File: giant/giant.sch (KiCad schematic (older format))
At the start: 55 parts, among them IC1 MC7805BDTRKG, J1 Conn_01x02, J2 Conn_01x01, J3 Conn_01x06

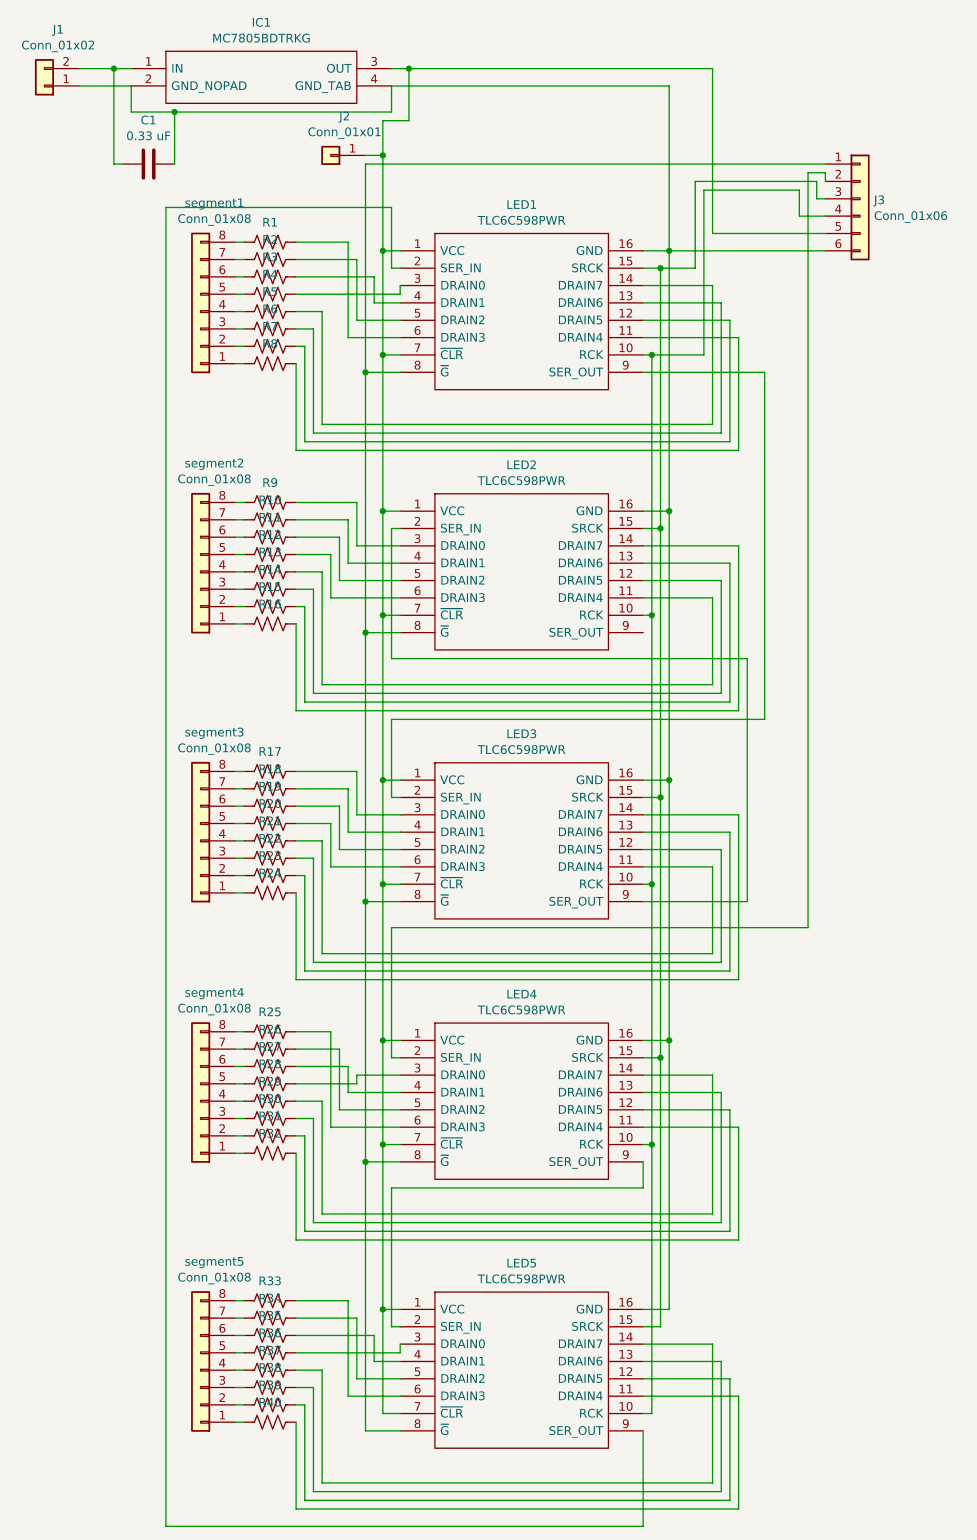
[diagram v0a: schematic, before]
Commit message: Improved schematic layout for both cleanliness and programming ease
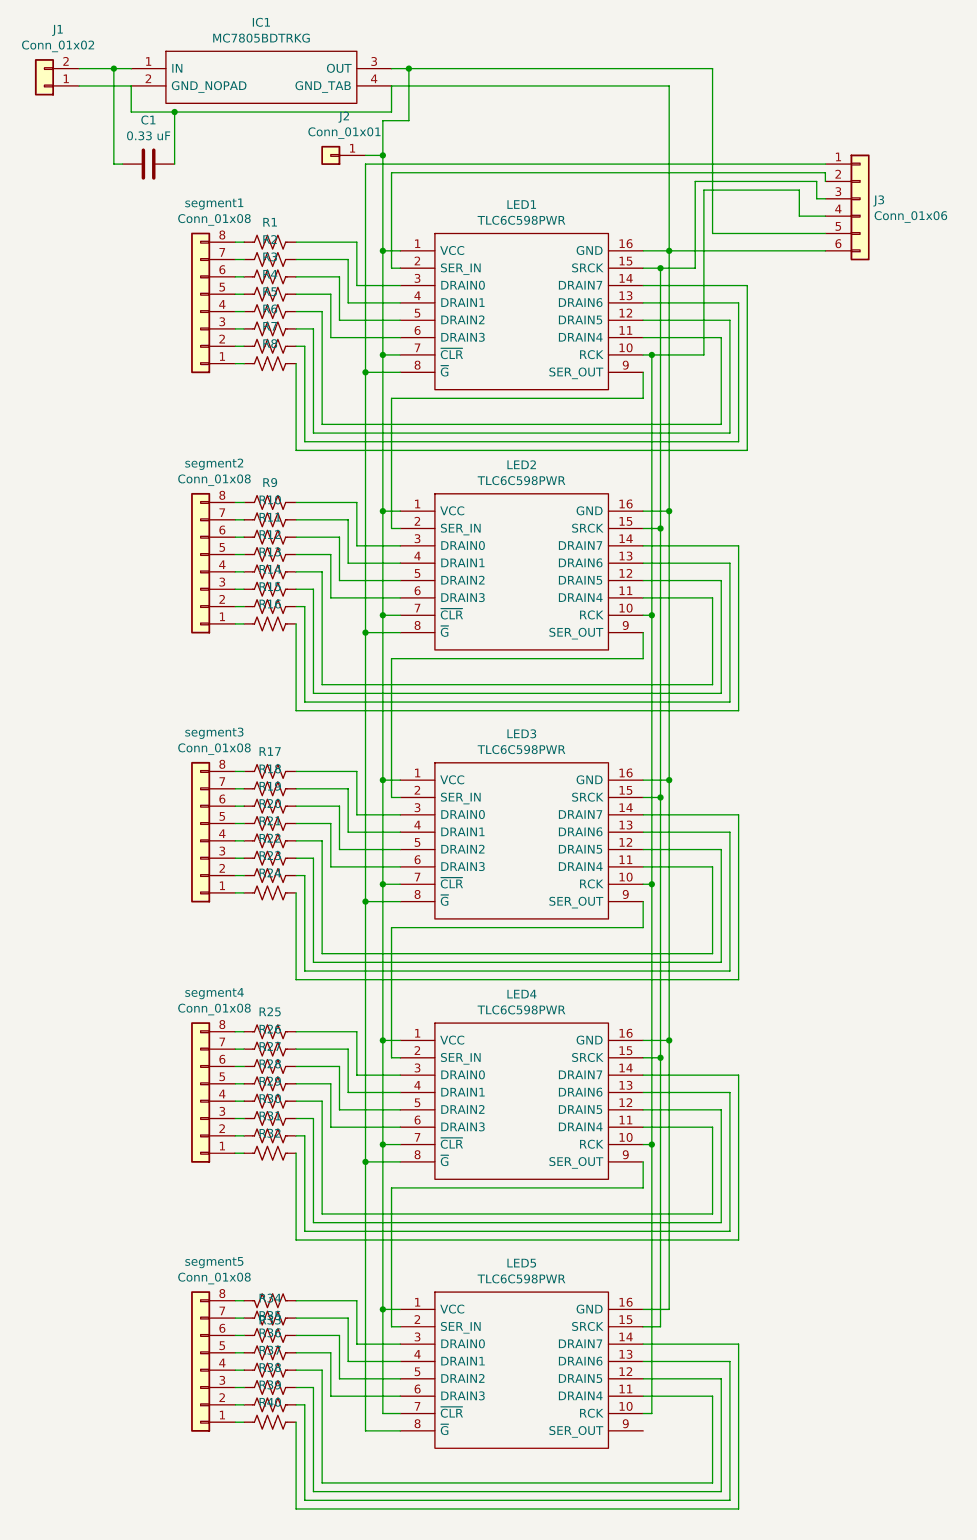
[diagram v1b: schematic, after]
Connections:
- net at LED5.11 (DRAIN4): now also R37.2; no longer R40.2
- net at LED5.12 (DRAIN5): now also R38.2; no longer R39.2
- net at LED5.13 (DRAIN6): now also R39.2; no longer R38.2
- net at LED5.14 (DRAIN7): now also R40.2; no longer R37.2
- net at LED5.3 (DRAIN0): now also R33.2; no longer R36.2
- net at LED5.4 (DRAIN1): now also R34.2; no longer R35.2
- net at LED5.5 (DRAIN2): now also R35.2; no longer R34.2
- net at LED5.6 (DRAIN3): now also R36.2; no longer R33.2
- net at LED5.9 (SER_OUT): no longer LED1.2 (SER_IN)
- net at LED4.11 (DRAIN4): now also R29.2; no longer R32.2
- net at LED4.12 (DRAIN5): now also R30.2; no longer R31.2
- net at LED4.13 (DRAIN6): now also R31.2; no longer R30.2
- net at LED4.14 (DRAIN7): now also R32.2; no longer R29.2
- net at LED4.2 (SER_IN): now also LED3.9 (SER_OUT); no longer J3.2 (Pin_2)
- net at LED4.3 (DRAIN0): now also R25.2; no longer R28.2
- net at LED4.4 (DRAIN1): now also R26.2; no longer R27.2
- net at LED4.5 (DRAIN2): now also R27.2; no longer R26.2
- net at LED4.6 (DRAIN3): now also R28.2; no longer R25.2
- net at LED3.2 (SER_IN): now also LED2.9 (SER_OUT); no longer LED1.9 (SER_OUT)
- net at LED2.2 (SER_IN): now also LED1.9 (SER_OUT); no longer LED3.9 (SER_OUT)
- net at LED1.11 (DRAIN4): now also R5.2; no longer R8.2
- net at LED1.12 (DRAIN5): now also R6.2; no longer R7.2
- net at LED1.13 (DRAIN6): now also R7.2; no longer R6.2
- net at LED1.14 (DRAIN7): now also R8.2; no longer R5.2
- net at LED1.3 (DRAIN0): now also R1.2; no longer R4.2
- net at LED1.4 (DRAIN1): now also R2.2; no longer R3.2
- net at LED1.5 (DRAIN2): now also R3.2; no longer R2.2
- net at LED1.6 (DRAIN3): now also R4.2; no longer R1.2
- new net: J3.2 (Pin_2), LED1.2 (SER_IN)
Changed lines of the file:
@@
 EESchema Schematic File Version 4
+LIBS:giant-cache
 EELAYER 26 0
 EELAYER END
@@
 Wire Wire Line
 	4100 8700 4100 8100
-$Comp
-L TLC6C598PWR:TLC6C598PWR LED4
-U 1 1 5C3858CA
-P 4200 6550
-F 0 "LED4" H 4900 6815 50  0000 C CNN
-F 1 "TLC6C598PWR" H 4900 6724 50  0000 C CNN
-F 2 "SOP65P640X120-16N" H 5450 6650 50  0001 L CNN
-F 3 "http://www.ti.com/lit/gpn/tlc6c598" H 5450 6550 50  0001 L CNN
-F 4 "TLC6C598 8-Bit Shift-Register LED Driver " H 5450 6450 50  0001 L CNN "Description"
-F 5 "1.2" H 5450 6350 50  0001 L CNN "Height"
-F 6 "Texas Instruments" H 5450 6250 50  0001 L CNN "Manufacturer_Name"
-F 7 "TLC6C598PWR" H 5450 6150 50  0001 L CNN "Manufacturer_Part_Number"
-F 8 "595-TLC6C598PWR" H 5450 5850 50  0001 L CNN "Mouser Part Number"
-F 9 "https://www.mouser.com/Search/Refine.aspx?Keyword=595-TLC6C598PWR" H 5450 5750 50  0001 L CNN "Mouser Price/Stock"
-	1    4200 6550
-	1    0    0    -1
-$EndComp
 Wire Wire Line
 	4200 6550 4100 6550
@@
 Connection ~ 4000 7250
 Wire Wire Line
-	4200 8200 4150 8200
-Wire Wire Line
-	4150 8200 4150 7400
-Wire Wire Line
-	4150 7400 5600 7400
-Wire Wire Line
-	5600 7400 5600 7250
-Wire Wire Line
-	4200 6650 4150 6650
-Wire Wire Line
-	4150 6650 4150 5900
-Wire Wire Line
 	4200 5150 4150 5150
-Wire Wire Line
-	4150 5150 4150 4700
 Wire Wire Line
 	5600 2600 5650 2600
@@
 	3300 1950 3250 1950
 Wire Wire Line
-	6000 3000 3750 3000
-Wire Wire Line
 	3750 3000 3750 2350
 Wire Wire Line
 	3750 2350 3600 2350
 Wire Wire Line
-	6050 3050 3700 3050
-Wire Wire Line
 	3700 3050 3700 2450
 Wire Wire Line
@@
 Wire Wire Line
 	3650 2550 3600 2550
-Wire Wire Line
-	3650 3100 6100 3100
 Connection ~ 4100 3500
 Connection ~ 4100 2600
@@
 Wire Wire Line
 	4000 1500 4000 2700
-Wire Wire Line
-	6150 3150 3600 3150
 Wire Wire Line
 	3600 3150 3600 2650
@@
 	3300 6500 3250 6500
 Wire Wire Line
-	3950 6750 4200 6750
-Wire Wire Line
-	4200 6850 3900 6850
-Wire Wire Line
-	3850 6950 4200 6950
-Wire Wire Line
-	4200 7050 3800 7050
-Wire Wire Line
 	3750 7550 3750 6900
 Wire Wire Line
@@
 F 4 "ESR10EZPJ201" H 3450 8050 50  0001 C CNN "PartNumber"
 	1    3450 8050
-	0    -1   -1   0
+	0    -1   1    0
 $EndComp
 $Comp
@@
 	4000 1500 6650 1500
 Wire Wire Line
-	6650 1550 6650 1600
-Wire Wire Line
 	6600 1600 6600 1700
 Wire Wire Line
@@
 	4100 1450 4100 2000
 Wire Wire Line
-	3800 6500 3600 6500
-Wire Wire Line
-	3800 6500 3800 7050
-Wire Wire Line
-	3850 6950 3850 6600
-Wire Wire Line
-	3850 6600 3600 6600
-Wire Wire Line
-	3900 6850 3900 6700
-Wire Wire Line
-	3900 6700 3600 6700
-Wire Wire Line
-	3950 6750 3950 6800
-Wire Wire Line
-	3950 6800 3600 6800
-Wire Wire Line
-	6000 6750 5600 6750
-Wire Wire Line
-	6000 6750 6000 7550
-Wire Wire Line
-	6050 7600 6050 6850
-Wire Wire Line
-	6050 6850 5600 6850
-Wire Wire Line
-	6100 7650 6100 6950
-Wire Wire Line
-	6100 6950 5600 6950
-Wire Wire Line
-	6150 7700 6150 7050
-Wire Wire Line
-	6150 7050 5600 7050
-Wire Wire Line
-	6000 9100 6000 8300
-Wire Wire Line
-	6000 8300 5600 8300
-Wire Wire Line
-	6050 9150 6050 8400
-Wire Wire Line
-	6050 8400 5600 8400
-Wire Wire Line
-	6100 9200 6100 8500
-Wire Wire Line
-	6100 8500 5600 8500
-Wire Wire Line
-	6150 9250 6150 8600
-Wire Wire Line
-	6150 8600 5600 8600
-Wire Wire Line
-	4200 8300 4200 8350
-Wire Wire Line
-	4200 8350 3600 8350
-Wire Wire Line
-	4200 8400 4050 8400
-Wire Wire Line
-	4050 8400 4050 8250
-Wire Wire Line
-	4050 8250 3600 8250
-Wire Wire Line
-	4200 8500 3950 8500
-Wire Wire Line
-	3950 8500 3950 8150
-Wire Wire Line
-	3950 8150 3600 8150
-Wire Wire Line
-	4200 8600 3900 8600
-Wire Wire Line
-	3900 8600 3900 8050
-Wire Wire Line
-	3900 8050 3600 8050
-Wire Wire Line
 	4200 5250 3950 5250
 Wire Wire Line
@@
 Wire Wire Line
 	3800 3750 3600 3750
-Wire Wire Line
-	4200 2200 4200 2250
-Wire Wire Line
-	4050 2300 4050 2150
-Wire Wire Line
-	4200 2300 4050 2300
-Wire Wire Line
-	4200 2500 3900 2500
-Wire Wire Line
-	4200 2400 3950 2400
-Wire Wire Line
-	3900 1950 3600 1950
-Wire Wire Line
-	3900 2500 3900 1950
-Wire Wire Line
-	3950 2050 3600 2050
-Wire Wire Line
-	3950 2400 3950 2050
-Wire Wire Line
-	4050 2150 3600 2150
-Wire Wire Line
-	4200 2250 3600 2250
-Wire Wire Line
-	6000 2200 5600 2200
-Wire Wire Line
-	6000 3000 6000 2200
-Wire Wire Line
-	6050 2300 5600 2300
-Wire Wire Line
-	6050 3050 6050 2300
-Wire Wire Line
-	6100 2400 5600 2400
-Wire Wire Line
-	6100 3100 6100 2400
-Wire Wire Line
-	6150 2500 6150 3150
-Wire Wire Line
-	5600 2500 6150 2500
-Wire Wire Line
-	5600 8800 5600 9350
-Wire Wire Line
-	5600 9350 2850 9350
-Wire Wire Line
-	2850 1750 2850 9350
-Wire Wire Line
-	4150 1750 4150 2100
-Wire Wire Line
-	4150 2100 4200 2100
-Wire Wire Line
-	2850 1750 4150 1750
 $Comp
 L TLC6C598PWR:TLC6C598PWR LED1
@@
 $EndComp
 Wire Wire Line
-	5600 2700 6300 2700
-Wire Wire Line
-	6300 2700 6300 4700
-Wire Wire Line
-	6300 4700 4150 4700
-Wire Wire Line
-	5600 5750 6200 5750
-Wire Wire Line
-	6200 5750 6200 4350
-Wire Wire Line
-	6200 4350 4150 4350
-Wire Wire Line
-	4150 4350 4150 3600
-Wire Wire Line
-	4150 3600 4200 3600
-Wire Wire Line
-	6550 5900 6550 1550
-Wire Wire Line
-	6550 1550 6650 1550
-Wire Wire Line
-	4150 5900 6550 5900
-Wire Wire Line
 	5750 1050 5750 2000
 Wire Wire Line
@@
 Wire Wire Line
 	5750 2000 6650 2000
+Wire Wire Line
+	3750 3000 6050 3000
+Wire Wire Line
+	5600 2500 6050 2500
+Wire Wire Line
+	6050 2500 6050 3000
+Wire Wire Line
+	6100 3050 6100 2400
+Wire Wire Line
+	6100 2400 5600 2400
+Wire Wire Line
+	3700 3050 6100 3050
+Wire Wire Line
+	5600 2300 6150 2300
+Wire Wire Line
+	6150 2300 6150 3100
+Wire Wire Line
+	3650 3100 6150 3100
+Wire Wire Line
+	5600 2200 6200 2200
+Wire Wire Line
+	6200 2200 6200 3150
+Wire Wire Line
+	3600 3150 6200 3150
+Wire Wire Line
+	3600 2250 3800 2250
+Wire Wire Line
+	3800 2250 3800 2500
+Wire Wire Line
+	3800 2500 4200 2500
+Wire Wire Line
+	4200 2400 3850 2400
+Wire Wire Line
+	3850 2400 3850 2150
+Wire Wire Line
+	3850 2150 3600 2150
+Wire Wire Line
+	3600 2050 3900 2050
+Wire Wire Line
+	3900 2050 3900 2300
+Wire Wire Line
+	3900 2300 4200 2300
+Wire Wire Line
+	4200 2200 3950 2200
+Wire Wire Line
+	3950 2200 3950 1950
+Wire Wire Line
+	3950 1950 3600 1950
+Wire Wire Line
+	5600 6750 6150 6750
+Wire Wire Line
+	6150 6750 6150 7700
+Wire Wire Line
+	6100 7650 6100 6850
+Wire Wire Line
+	6100 6850 5600 6850
+Wire Wire Line
+	6050 7600 6050 6950
+Wire Wire Line
+	6050 6950 5600 6950
+Wire Wire Line
+	6000 7550 6000 7050
+Wire Wire Line
+	6000 7050 5600 7050
+Wire Wire Line
+	4200 7050 3800 7050
+Wire Wire Line
+	3800 7050 3800 6800
+Wire Wire Line
+	3800 6800 3600 6800
+Wire Wire Line
+	3600 6700 3850 6700
+Wire Wire Line
+	3850 6700 3850 6950
+Wire Wire Line
+	3850 6950 4200 6950
+Wire Wire Line
+	3600 6600 3900 6600
+Wire Wire Line
+	3900 6600 3900 6850
+Wire Wire Line
+	3900 6850 4200 6850
+Wire Wire Line
+	4200 6750 3950 6750
+Wire Wire Line
+	3950 6750 3950 6500
+Wire Wire Line
+	3950 6500 3600 6500
+$Comp
+L TLC6C598PWR:TLC6C598PWR LED4
+U 1 1 5C3858CA
+P 4200 6550
+F 0 "LED4" H 4900 6815 50  0000 C CNN
+F 1 "TLC6C598PWR" H 4900 6724 50  0000 C CNN
+F 2 "SOP65P640X120-16N" H 5450 6650 50  0001 L CNN
+F 3 "http://www.ti.com/lit/gpn/tlc6c598" H 5450 6550 50  0001 L CNN
+F 4 "TLC6C598 8-Bit Shift-Register LED Driver " H 5450 6450 50  0001 L CNN "Description"
+F 5 "1.2" H 5450 6350 50  0001 L CNN "Height"
+F 6 "Texas Instruments" H 5450 6250 50  0001 L CNN "Manufacturer_Name"
+F 7 "TLC6C598PWR" H 5450 6150 50  0001 L CNN "Manufacturer_Part_Number"
+F 8 "595-TLC6C598PWR" H 5450 5850 50  0001 L CNN "Mouser Part Number"
+F 9 "https://www.mouser.com/Search/Refine.aspx?Keyword=595-TLC6C598PWR" H 5450 5750 50  0001 L CNN "Mouser Price/Stock"
+	1    4200 6550
+	1    0    0    -1
+$EndComp
+Wire Wire Line
+	5600 7250 5600 7400
+Wire Wire Line
+	5600 7400 4150 7400
+Wire Wire Line
+	4150 7400 4150 8200
+Wire Wire Line
+	4150 8200 4200 8200
+Wire Wire Line
+	4200 6650 4150 6650
+Wire Wire Line
+	4150 6650 4150 5900
+Wire Wire Line
+	4150 5900 5600 5900
+Wire Wire Line
+	5600 5900 5600 5750
+Wire Wire Line
+	4150 5150 4150 4350
+Wire Wire Line
+	4150 4350 5600 4350
+Wire Wire Line
+	5600 4350 5600 4200
+Wire Wire Line
+	4200 3600 4150 3600
+Wire Wire Line
+	4150 3600 4150 2850
+Wire Wire Line
+	4150 2850 5600 2850
+Wire Wire Line
+	5600 2850 5600 2700
+Wire Wire Line
+	4200 2100 4150 2100
+Wire Wire Line
+	4150 2100 4150 1550
+Wire Wire Line
+	4150 1550 6650 1550
+Wire Wire Line
+	6650 1550 6650 1600
+Wire Wire Line
+	4200 8300 3950 8300
+Wire Wire Line
+	3950 8300 3950 8050
+Wire Wire Line
+	3950 8050 3600 8050
+Wire Wire Line
+	3600 8150 3900 8150
+Wire Wire Line
+	3900 8150 3900 8400
+Wire Wire Line
+	3900 8400 4200 8400
+Wire Wire Line
+	4200 8500 3850 8500
+Wire Wire Line
+	3850 8500 3850 8250
+Wire Wire Line
+	3850 8250 3600 8250
+Wire Wire Line
+	3600 8350 3800 8350
+Wire Wire Line
+	3800 8350 3800 8600
+Wire Wire Line
+	3800 8600 4200 8600
+Wire Wire Line
+	6000 9100 6000 8600
+Wire Wire Line
+	6000 8600 5600 8600
+Wire Wire Line
+	5600 8500 6050 8500
+Wire Wire Line
+	6050 8500 6050 9150
+Wire Wire Line
+	5600 8400 6100 8400
+Wire Wire Line
+	6100 8400 6100 9200
+Wire Wire Line
+	5600 8300 6150 8300
+Wire Wire Line
+	6150 8300 6150 9250
 $EndSCHEMATC
